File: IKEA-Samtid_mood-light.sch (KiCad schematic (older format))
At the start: 24 parts, among them IC1 ATMEGA168PA-M, P1 FTDI, P2 POWER, P3.1 B-to-B-1A, P3.2 B-to-B-1B, P4.1 B-to-B-2A, P4.2 B-to-B-2B, Q1 BSS138, Q2 BSS138, SW1 ENTER, SW2 MODE, X1 CSTCE16M0V53-R0

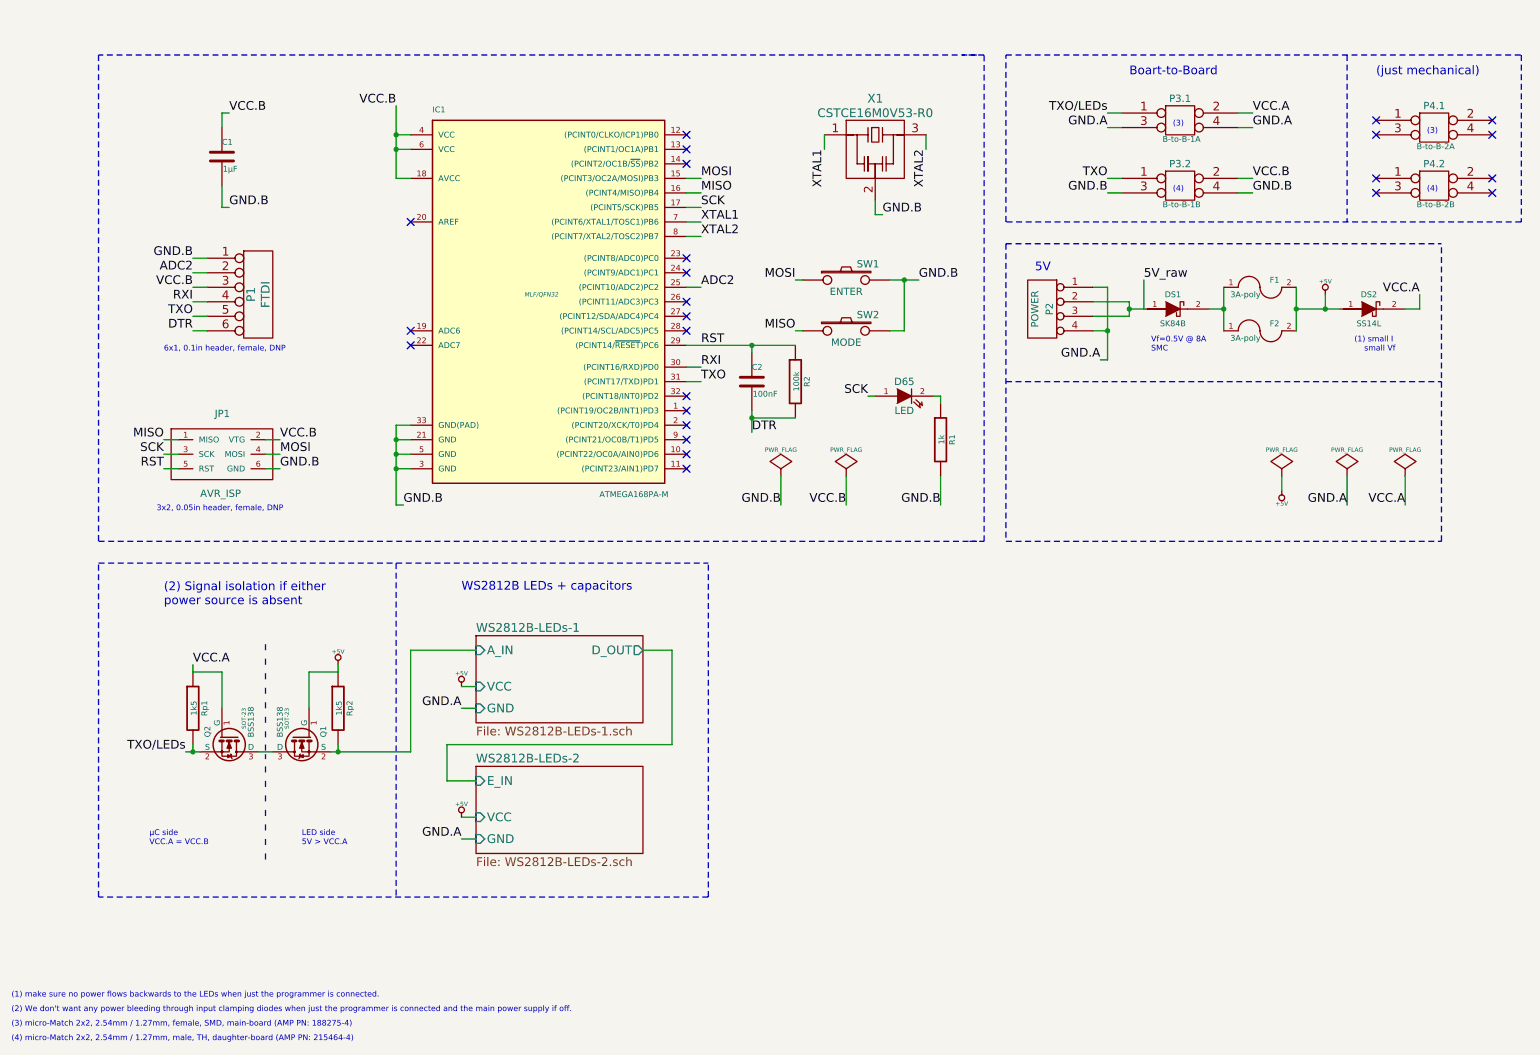
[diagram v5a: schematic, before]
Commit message: Reverse-polarity protection: replaced SK84 with 2x p-ch mosfets.
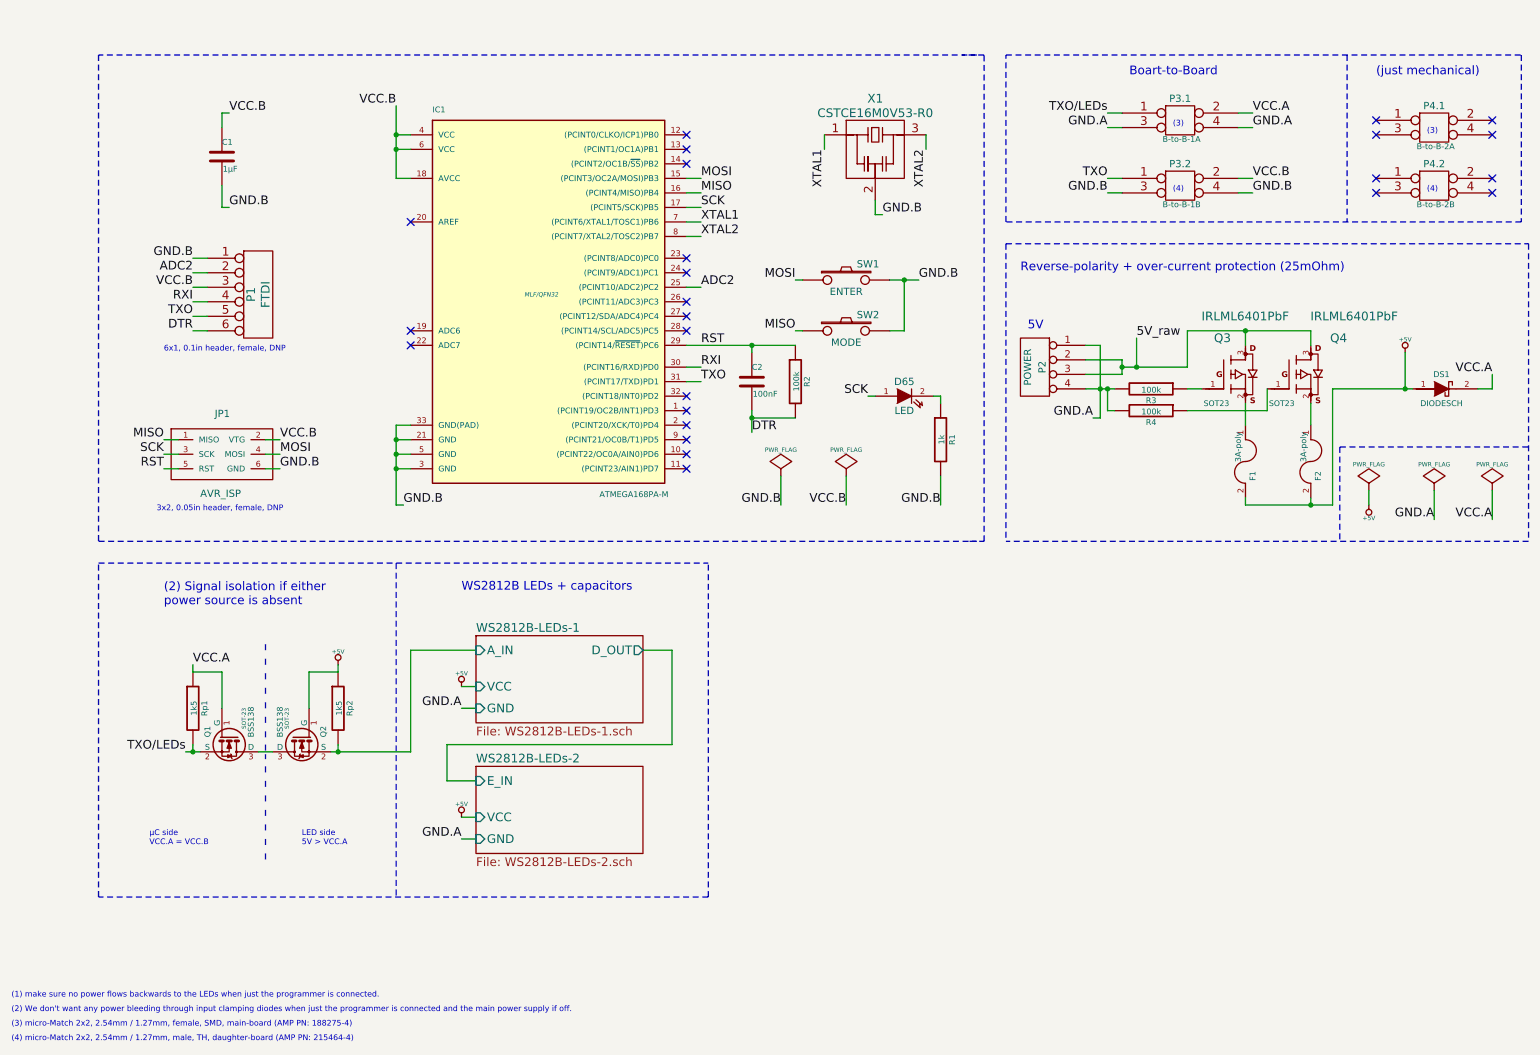
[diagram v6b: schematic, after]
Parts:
- removed DS2: SS14L, symbol DIODESCH
- added Q3, Q4: IRLML6401PbF, SOT23, symbol MOSFET_P
- added R3, R4: 100k, symbol R
- DS1: value SK84B -> DIODESCH
- renumbered Q2 to Q1, Q1 to Q2
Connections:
- net +5V: now also DS1.1 (A)
- net 5V_raw: now also Q3.3 (D), Q4.3 (D); no longer DS1.1 (A)
- net GND.A: now also R3.2, R4.2
- net VCC.A: now also DS1.2 (C)
- new net: F1.1, Q3.2 (S)
- new net: F2.1, Q4.2 (S)
- new net: Q3.1 (G), R3.1
- new net: Q4.1 (G), R4.1
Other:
- note added: "Reverse-polarity + over-current protection (25mOhm)"
- note removed: "(1) small I\n small Vf"
- note removed: "Vf=0.5V @ 8A\nSMC"
- moved on the sheet: F1, F2, P2

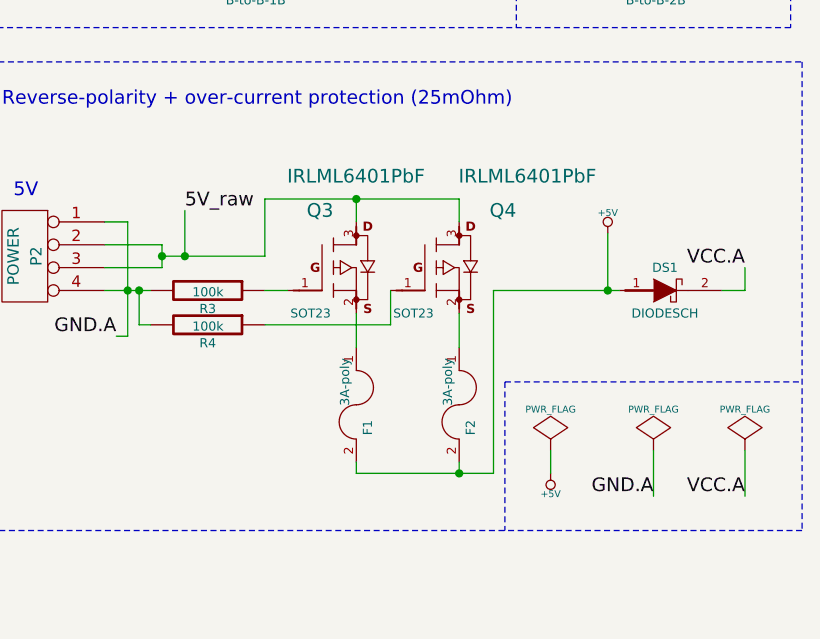
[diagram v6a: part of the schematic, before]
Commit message: 1x 3A poly-fuse is enough (just 20mOhm @ 2.6A).
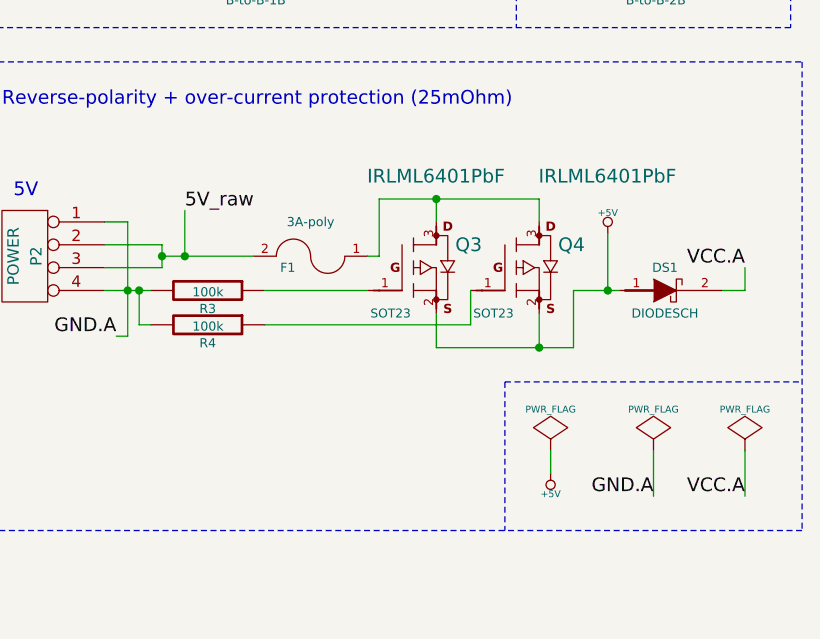
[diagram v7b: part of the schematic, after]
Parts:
- removed F2: 3A-poly, symbol FUSE
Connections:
- net +5V: now also Q3.2 (S), Q4.2 (S); no longer F1.2
- net 5V_raw: now also F1.2; no longer Q3.3 (D), Q4.3 (D)
- net at F1.1: now also Q3.3 (D), Q4.3 (D); no longer Q3.2 (S)
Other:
- moved on the sheet: F1, Q3, Q4
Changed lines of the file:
@@
 Sheet 1 3
 Title "IKEA-Samtid_mood-light"
-Date "24 Aug 2014"
-Rev "0.30"
+Date "25 Aug 2014"
+Rev "0.31"
 Comp "2014 - blog.spitzenpfeil.org"
 Comment1 ""
@@
 L FUSE F1
 U 1 1 53C3478B
-P 9050 3700
-F 0 "F1" H 9150 3750 40  0000 C CNN
-F 1 "3A-poly" H 8950 3650 40  0000 C CNN
-F 2 "" H 9050 3700 60  0000 C CNN
-F 3 "" H 9050 3700 60  0000 C CNN
-	1    9050 3700
-	0    1    1    0
-$EndComp
-$Comp
-L FUSE F2
-U 1 1 53C34893
-P 9500 3700
-F 0 "F2" H 9600 3750 40  0000 C CNN
-F 1 "3A-poly" H 9400 3650 40  0000 C CNN
-F 2 "" H 9500 3700 60  0000 C CNN
-F 3 "" H 9500 3700 60  0000 C CNN
-	1    9500 3700
-	0    1    1    0
+P 8850 3050
+F 0 "F1" H 8950 3100 40  0000 C CNN
+F 1 "3A-poly" H 8850 2900 40  0000 C CNN
+F 2 "" H 8850 3050 60  0000 C CNN
+F 3 "" H 8850 3050 60  0000 C CNN
+	1    8850 3050
+	-1   0    0    1
 $EndComp
 $Comp
@@
 	8050 2900 8050 3400
 Connection ~ 8050 3200
-Wire Wire Line
-	8200 3050 8650 3050
 Connection ~ 8200 3050
 Wire Wire Line
@@
 L MOSFET_P Q3
 U 1 1 53FA015D
-P 8750 3200
-F 0 "Q3" H 8950 3550 60  0000 R CNN
-F 1 "IRLML6401PbF" H 9350 3700 60  0000 R CNN
-F 2 "SOT23" H 8850 3100 39  0000 C CNN
-F 3 "" H 8750 3200 60  0000 C CNN
-	1    8750 3200
+P 9100 3200
+F 0 "Q3" H 9600 3400 60  0000 R CNN
+F 1 "IRLML6401PbF" H 9700 3700 60  0000 R CNN
+F 2 "SOT23" H 9200 3100 39  0000 C CNN
+F 3 "" H 9100 3200 60  0000 C CNN
+	1    9100 3200
 	1    0    0    -1
 $EndComp
@@
 L MOSFET_P Q4
 U 1 1 53FA1783
-P 9200 3200
-F 0 "Q4" H 9750 3550 60  0000 R CNN
-F 1 "IRLML6401PbF" H 10100 3700 60  0000 R CNN
-F 2 "SOT23" H 9300 3100 39  0000 C CNN
-F 3 "" H 9200 3200 60  0000 C CNN
-	1    9200 3200
-	1    0    0    -1
-$EndComp
-Wire Wire Line
-	9050 2900 9050 2800
-Wire Wire Line
-	9500 2800 9500 2900
-Wire Wire Line
-	9050 3300 9050 3450
-Wire Wire Line
-	8650 3050 8650 2800
+P 9550 3200
+F 0 "Q4" H 10050 3400 60  0000 R CNN
+F 1 "IRLML6401PbF" H 10450 3700 60  0000 R CNN
+F 2 "SOT23" H 9650 3100 39  0000 C CNN
+F 3 "" H 9550 3200 60  0000 C CNN
+	1    9550 3200
+	1    0    0    -1
+$EndComp
+Wire Wire Line
+	9400 2900 9400 2800
+Wire Wire Line
+	9850 2800 9850 2900
+Wire Wire Line
+	9400 3300 9400 3450
 Connection ~ 8300 3050
-Connection ~ 9050 2800
+Connection ~ 9400 2800
 $Comp
 L R R3
@@
 	8100 3200 8100 3350
 Wire Wire Line
-	8650 3200 8750 3200
+	8650 3200 9100 3200
 Connection ~ 8100 3200
 Wire Wire Line
@@
 $EndComp
 Wire Wire Line
-	8650 2800 9500 2800
-Wire Wire Line
-	9200 3200 9200 3350
-Wire Wire Line
-	9200 3350 8650 3350
+	9550 3350 9550 3200
+Wire Wire Line
+	8650 3350 9550 3350
 Wire Wire Line
 	10150 2950 10150 3200
@@
 Reverse-polarity + over-current protection (25mOhm)
 Wire Wire Line
-	9500 3300 9500 3450
-Wire Wire Line
-	9050 3950 9050 4000
-Wire Wire Line
-	9050 4000 9650 4000
-Wire Wire Line
-	9500 4000 9500 3950
-Wire Wire Line
-	9650 4000 9650 3200
-Connection ~ 9500 4000
+	9850 3300 9850 3450
 Connection ~ 10150 3200
 Wire Wire Line
-	9650 3200 10200 3200
+	9400 3450 10000 3450
+Connection ~ 9850 3450
+Wire Wire Line
+	9150 2800 9850 2800
+Wire Wire Line
+	10000 3200 10200 3200
+Wire Wire Line
+	10000 3450 10000 3200
+Wire Wire Line
+	9150 2800 9150 3050
+Wire Wire Line
+	9150 3050 9100 3050
+Wire Wire Line
+	8200 3050 8600 3050
 $EndSCHEMATC

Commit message: Being creative...
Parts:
- added U1: AP2204K-SOT23-5, my_parts:MADW__SOT23-5, symbol MADW__AP2204K-SOT23-5
- C1, C2: footprint (none) -> my_parts:MADW__C0805
- D65: footprint (none) -> my_parts:MADW__CHIPLED-0603
- DS1: footprint (none) -> my_parts:MADW__diode_sub-SMA
- F1: footprint (none) -> my_parts:MADW__R1206
- IC1: footprint MLF/QFN32 -> SMD_Packages:QFN-32-1EP
- JP1: footprint (none) -> my_parts:MADW__PIN_ARRAY_3x2_1.27mm
- P1: footprint (none) -> my_parts:MADW__SIL-6
- P2: footprint (none) -> my_parts:MADW__SIL-4
- P3.1, P4.1: footprint (none) -> micro-MaTch:0-188275-4_SMD_4-pin_female_split-pads
- P3.2, P4.2: footprint (none) -> micro-MaTch:0-215464-4_TH_4-pin_male
- Q1, Q2: footprint SOT-23 -> my_parts:MADW__SOT23
- Q3, Q4: footprint SOT23 -> my_parts:MADW__SOT23
- R1, R2, R3, R4, Rp1, Rp2: footprint (none) -> my_parts:MADW__R0603_2
- SW1, SW2: footprint (none) -> my_parts:MADW__push-button-SMD-3.7x6.0
- X1: footprint (none) -> my_parts:MADW__murata-resonator__CSTCE16M0V53-R0
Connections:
- net RXI is gone; now on net RXI.B: IC1.30 ((PCINT16/RXD)PD0), P1.4
- net +5V: now also U1.1 (Vin), U1.3 (EN); no longer DS1.1 (A)
- net GND.A: now also U1.2 (GND)
- net VCC.A: now also U1.5 (OUT); no longer DS1.2 (C)
- net VCC.B: now also DS1.1 (A); no longer C1.1, IC1.18 (AVCC), IC1.4 (VCC), IC1.6 (VCC), JP1.2 (VTG), P1.3
- net LEDS.B: now reaches IC1.9 ((PCINT21/OC0B/T1)PD5)
- net LEDS.B: now also P3.2.1
- net RXI.A: now reaches P4.1.1
- net TXO.A: now reaches P4.1.3
- net RXI.B: now reaches P4.2.1
- net TXO.B: now reaches P4.2.3
- net TXO.B: now also IC1.31 ((PCINT17/TXD)PD1), P1.5
- removed net TXO: IC1.31 ((PCINT17/TXD)PD1), P1.5, P3.2.1
- net TXO/LEDs renamed LEDS.A
- new net VCC.B2: C1.1, DS1.2 (C), IC1.18 (AVCC), IC1.4 (VCC), IC1.6 (VCC), JP1.2 (VTG), P1.3
- no-connect marks 25 -> 21
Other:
- note added: "(3.3V)"
- note added: "prevent backfeeding of power"
- note removed: "(just mechanical)"
- moved on the sheet: C1, C2, DS1, F1, P1, P2, P3.1, P3.2, P4.1, P4.2, Q3, Q4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
